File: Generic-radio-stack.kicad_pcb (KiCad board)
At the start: 2 copper layers, 104 parts, among them J1 USB_B_Mini, J2 Conn_01x02, SW1 SW_Push_LED, SW2 SW_Push_LED, SW3 SW_Push_LED, SW4 SW_Push_LED, U1 NCP1117-3.3_SOT223, U10 MAX7219, U11 5_digit_7_segment_display, U12 MAX7219, U13 5_digit_7_segment_display, U14 MAX7219, U15 5_digit_7_segment_display, U16 MAX7219, U17 5_digit_7_segment_display, U18 RP2040, U19 LSF0204PWR, U2 MAX7219, U20 W25Q128JVS, U3 6_digit_7_segment_display_1, U4 MAX7219, U5 6_digit_7_segment_display_1, U6 MAX7219, U7 6_digit_7_segment_display_1, U8 MAX7219, U9 6_digit_7_segment_display_1, Y1 ABLS-12.000MHZ-B4-T

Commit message: Board layout begins. Ugh.
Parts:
- C10, C11, C12, C13, C14, C15, C16, C17, C18, C3, C4, C5, C6, C7, C8, C9, R1, R10, R11, R12, R13, R14, R15, R16, R17, R2, R3, R4, U10, U12, U14, U16, U2, U4, U6, U8: moved to B.Cu
- moved C2 269.2 mm to (462.8, 121.3)
- moved C24 269.2 mm to (477.8, 136.3)
- moved C29 269.2 mm to (471.5, 140.4)
- moved C31 269.2 mm to (471.5, 142.4)
- moved ENC1 269.2 mm to (404.9, 131.2)
- moved R21 269.2 mm to (416.7, 120.4)
- moved R28 269.2 mm to (477.8, 138.3)
- moved R37 269.2 mm to (471.5, 144.5)
- moved U18 269.2 mm to (475.2, 130.6)
- moved U19 269.2 mm to (459.3, 142.3)
- moved C19 269.2 mm to (465.2, 142.5)
- moved C21 269.2 mm to (468.4, 142.5)
- moved C22 269.2 mm to (465.2, 140.4)
- moved C23 269.2 mm to (474.6, 138.3)
- moved C25 269.2 mm to (487.7, 127.0)
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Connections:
- R2 pad 1: COM2_INPUT -> (no net)
- R2 pad 2: Net-(D2-Pad2) -> (no net)
- SW3 pad 1: GND -> (no net)
- SW3 pad 2: COM2_XFR -> (no net)
- SW3 pad 3: Net-(R8-Pad2) -> (no net)
- SW3 pad 4: GND -> (no net)
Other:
- board outline added: 225 x 60 mm

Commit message: Added dual encoder 3d model, fit everything on the board
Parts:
- removed the U8 at (111.9, 96.3)
- added U12: 5_digit_7_segment_display, Generic-radio-stack:5 digit (3+2) 7 segment LED display, F.Cu at (169.0, 65.0)
- C1, C19, C2, C20, C21, C22, C23, C24, C25, C26, C27, C28, C29, C30, C31, C32, D5, J1, J2, R18, R19, R20, R21, R22, R23, R24, R25, R26, R27, R28, R29, R30, R31, R32, R33, R34, R35, R36, R37, R38, R5, R6, R7, R8, R9, Y1: moved to B.Cu
- D1, D2, D3, D4: footprint LED_THT:LED_D5.0mm -> LED_THT:LED_D3.0mm
- U10: value MAX7219 -> 6_digit_7_segment_display_1; footprint Package_SO:SOIC-24W_7.5x15.4mm_P1.27mm -> Generic-radio-stack:6 digit (3+3) 7 segment LED display; moved to F.Cu
- U11: value 5_digit_7_segment_display -> MAX7219; footprint Generic-radio-stack:5 digit (3+2) 7 segment LED display -> Package_SO:SOIC-24W_7.5x15.4mm_P1.27mm; moved to B.Cu
- U19: renamed from U18; moved to B.Cu
- U2: renamed from U1; moved to B.Cu
- U20: renamed from U19; moved to B.Cu
- U21: renamed from U20; moved to B.Cu
- U9: value 6_digit_7_segment_display_1 -> MAX7219; footprint Generic-radio-stack:6 digit (3+3) 7 segment LED display -> Package_SO:SOIC-24W_7.5x15.4mm_P1.27mm; moved to B.Cu
- moved R8 408.8 mm to (89.5, 84.0), turned to 180 degrees
- moved R6 407.1 mm to (89.4, 65.0), turned to 180 degrees
- moved C1 367.0 mm to (123.0, 51.5), turned to -90 degrees
- moved C25 366.6 mm to (122.9, 90.7), turned to 180 degrees
- moved C20 360.3 mm to (126.0, 92.8), turned to 180 degrees
- moved R34 360.3 mm to (126.0, 94.8), turned to 180 degrees
- moved R38 360.3 mm to (126.0, 90.7), turned to 180 degrees
- moved U2 355.5 mm to (129.0, 51.5), turned to 180 degrees
- moved C26 354.1 mm to (129.2, 94.8), turned to 180 degrees
- moved C27 354.1 mm to (129.2, 92.8), turned to 180 degrees
- moved R29 354.1 mm to (129.2, 96.9), turned to 180 degrees
- moved R36 354.1 mm to (129.2, 90.7), turned to 180 degrees
- moved R31 353.2 mm to (129.6, 100.0), turned to 180 degrees
- moved R5 352.6 mm to (149.0, 50.5), turned to 90 degrees
- moved C24 346.9 mm to (132.8, 100.0), turned to 180 degrees
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- renumbered U12 to U13, U13 to U14, U14 to U15, U15 to U16, U16 to U17, U17 to U18, U2 to U3, U3 to U4, U4 to U5, U5 to U6, U6 to U7, U7 to U8
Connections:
- R2 pad 1: (no net) -> COM2_INPUT
- R2 pad 2: (no net) -> Net-(D2-Pad2)
- SW3 pad 1: (no net) -> GND
- SW3 pad 2: (no net) -> COM2_XFR
- SW3 pad 3: (no net) -> Net-(R8-Pad2)
- SW3 pad 4: (no net) -> GND
- U10 pad 1: /5-digit display/DIN -> /6-digit display3/E
- U10 pad 10: unconnected-(U10-Pad10) -> /6-digit display3/F
- U10 pad 11: /5-digit display/DIG_1 -> /6-digit display3/A
- U10 pad 12: LED_LOAD -> /6-digit display3/DIG_5
- U10 pad 13: LED_CLOCK -> /6-digit display3/E
- U10 pad 14: /5-digit display/A -> /6-digit display3/D
- U10 pad 15: /5-digit display/F -> /6-digit display3/DP
- U10 pad 16: /5-digit display/B -> /6-digit display3/C
- U10 pad 17: /5-digit display/G -> /6-digit display3/G
- U10 pad 19: +5V -> /6-digit display3/B
- U10 pad 2: /5-digit display/DIG_0 -> /6-digit display3/D
- U10 pad 20: /5-digit display/C -> /6-digit display3/DIG_0
- U10 pad 21: /5-digit display/E -> /6-digit display3/DIG_1
- U10 pad 22: /5-digit display/DP -> /6-digit display3/F
- U10 pad 23: /5-digit display/D -> /6-digit display3/A
- U10 pad 24: /5-digit display/DOUT -> /6-digit display3/DIG_2
- U10 pad 3: /5-digit display/DIG_4 -> /6-digit display3/DP
- U10 pad 4: GND -> /6-digit display3/C
- U10 pad 5: unconnected-(U10-Pad5) -> /6-digit display3/G
- U10 pad 7: /5-digit display/DIG_3 -> /6-digit display3/B
- U10 pad 8: unconnected-(U10-Pad8) -> /6-digit display3/DIG_3
- U10 pad 9: GND -> /6-digit display3/DIG_4
- U11 pad 1: /5-digit display/E -> /5-digit display/DIN
- U11 pad 10: /5-digit display/F -> unconnected-(U11-Pad10)
- U11 pad 11: /5-digit display/A -> /5-digit display/DIG_1
- U11 pad 12: /5-digit display/DIG_4 -> LED_LOAD
- U11 pad 13: /5-digit display/E -> LED_CLOCK
- U11 pad 14: /5-digit display/D -> /5-digit display/A
- U11 pad 15: /5-digit display/C -> /5-digit display/F
- U11 pad 16: /5-digit display/G -> /5-digit display/B
- U11 pad 17: /5-digit display/DP -> /5-digit display/G
- U11 pad 18: /5-digit display/DIG_0 -> Net-(R14-Pad1)
- U11 pad 19: /5-digit display/A -> +5V
- U11 pad 2: /5-digit display/D -> /5-digit display/DIG_0
- U11 pad 20: /5-digit display/B -> /5-digit display/C
- U11 pad 21: /5-digit display/DIG_1 -> /5-digit display/E
- U11 pad 22: /5-digit display/F -> /5-digit display/DP
- U11 pad 3: /5-digit display/DP -> /5-digit display/DIG_4
- U11 pad 4: /5-digit display/C -> GND
- U11 pad 5: /5-digit display/G -> unconnected-(U11-Pad5)
- U11 pad 7: /5-digit display/B -> /5-digit display/DIG_3
- U11 pad 8: /5-digit display/DIG_2 -> unconnected-(U11-Pad8)
- U11 pad 9: /5-digit display/DIG_3 -> GND
- U9 pad 1: /6-digit display3/E -> /6-digit display2/DOUT
- U9 pad 10: /6-digit display3/F -> /6-digit display3/DIG_5
- U9 pad 11: /6-digit display3/A -> /6-digit display3/DIG_1
- U9 pad 12: /6-digit display3/DIG_5 -> LED_LOAD
- U9 pad 13: /6-digit display3/E -> LED_CLOCK
- U9 pad 14: /6-digit display3/D -> /6-digit display3/A
- U9 pad 15: /6-digit display3/DP -> /6-digit display3/F
- U9 pad 16: /6-digit display3/C -> /6-digit display3/B
- U9 pad 19: /6-digit display3/B -> +5V
- U9 pad 2: /6-digit display3/D -> /6-digit display3/DIG_0
- U9 pad 20: /6-digit display3/DIG_0 -> /6-digit display3/C
- U9 pad 21: /6-digit display3/DIG_1 -> /6-digit display3/E
- U9 pad 22: /6-digit display3/F -> /6-digit display3/DP
- U9 pad 23: /6-digit display3/A -> /6-digit display3/D
- U9 pad 24: /6-digit display3/DIG_2 -> /5-digit display3/DIN
- U9 pad 3: /6-digit display3/DP -> /6-digit display3/DIG_4
- U9 pad 4: /6-digit display3/C -> GND
- U9 pad 5: /6-digit display3/G -> unconnected-(U9-Pad5)
- U9 pad 7: /6-digit display3/B -> /6-digit display3/DIG_3
- U9 pad 8: /6-digit display3/DIG_3 -> unconnected-(U9-Pad8)
- U9 pad 9: /6-digit display3/DIG_4 -> GND
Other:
- board size 225 x 60 mm -> 225 x 66.5 mm

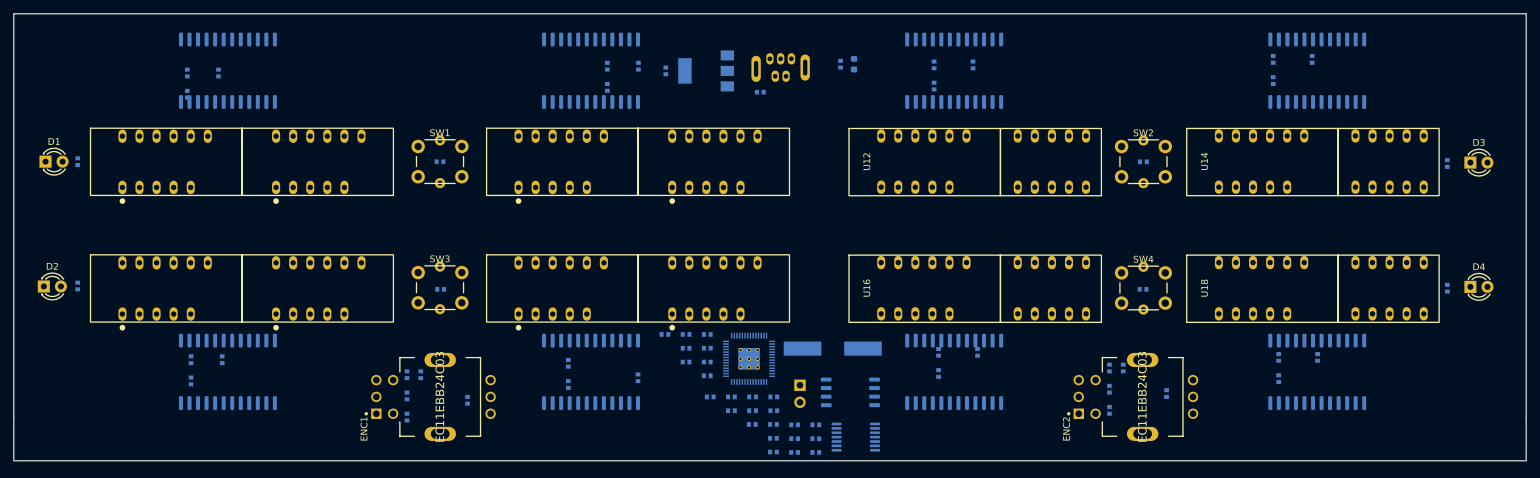
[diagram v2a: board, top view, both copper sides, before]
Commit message: Add mounting holes
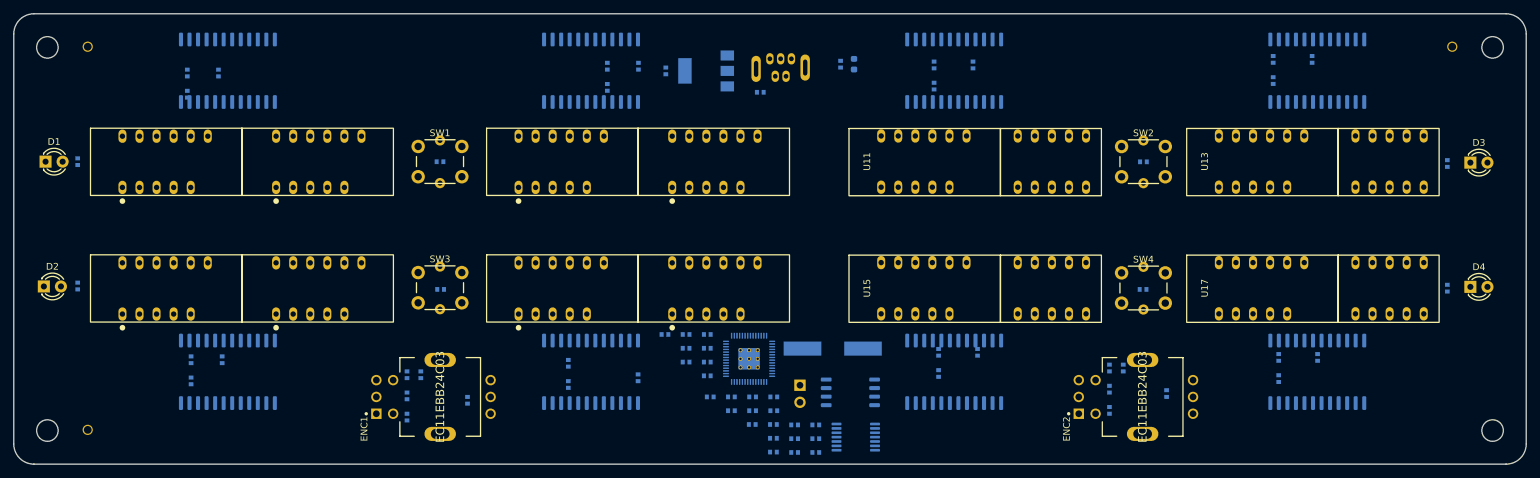
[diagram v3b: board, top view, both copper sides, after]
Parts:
- added H1: MountingHole, MountingHole:MountingHole_3.2mm_M3, F.Cu at (31.0, 48.0)
- added H2: MountingHole, MountingHole:MountingHole_3.2mm_M3, F.Cu at (246.0, 48.0)
- added H3: MountingHole, MountingHole:MountingHole_3.2mm_M3, F.Cu at (31.0, 105.0)
- added H4: MountingHole, MountingHole:MountingHole_3.2mm_M3, F.Cu at (246.0, 105.0)
- added H5: MountingHole, Generic-radio-stack:JLCPCB_Tooling_Hole, F.Cu at (37.0, 48.0)
- added H6: MountingHole, Generic-radio-stack:JLCPCB_Tooling_Hole, F.Cu at (240.0, 48.0)
- added H7: MountingHole, Generic-radio-stack:JLCPCB_Tooling_Hole, F.Cu at (37.0, 105.0)
- renumbered U2 to U1, U11 to U10, U12 to U11, U13 to U12, U14 to U13, U15 to U14, U16 to U15, U17 to U16, U18 to U17, U19 to U18, U20 to U19, U3 to U2, U21 to U20, U4 to U3, U5 to U4, U6 to U5, U7 to U6, U8 to U7, U9 to U8, U10 to U9
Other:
- board size 225 x 66.5 mm -> 225 x 67 mm

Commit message: initial routing of RP2040
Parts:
- moved J2 246.8 mm to (388.7, 121.3)
- moved R31 225.7 mm to (355.1, 110.5)
- moved R34 217.4 mm to (342.4, 115.6)
- moved R38 213.4 mm to (338.1, 114.6)
- moved R36 210.4 mm to (338.6, 111.3)
- moved R37 203.4 mm to (342.4, 112.3)
- moved U19 197.9 mm to (349.0, 112.8)
- moved R32 197.4 mm to (342.7, 110.2)
- moved R33 182.0 mm to (323.3, 121.4)
- moved R35 180.5 mm to (315.5, 122.2)
- moved C32 177.1 mm to (318.8, 121.2)
- moved U20 171.9 mm to (320.0, 127.3)
- moved C20 61.3 mm to (158.6, 144.7), turned to 0 degrees
- moved Y1 58.2 mm to (159.8, 149.8)
- moved C27 56.2 mm to (164.7, 136.3), turned to 0 degrees
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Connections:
- net Net-(R28-Pad2) renamed /RP2040/XOUT
- net Net-(R29-Pad1) renamed /RP2040/D+
- net Net-(R30-Pad1) renamed /RP2040/D-
- C19 pad 2: Net-(C19-Pad2) -> /RP2040/XIN
- U18 pad 20: Net-(C19-Pad2) -> /RP2040/XIN
- U18 pad 44: GND -> +3V3
- Y1 pad 1: Net-(C20-Pad2) -> /RP2040/XIN
- Y1 pad 2: Net-(C19-Pad2) -> Net-(C20-Pad2)
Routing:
- net +3V3: track 0.00 -> 28.5 mm
- net +1V1: track 0.00 -> 18.7 mm, vias 0 -> 4
- net /RP2040/XIN: track 0.00 -> 13.3 mm
- net Net-(C20-Pad2): track 0.00 -> 8.12 mm
- net /RP2040/XOUT: track 0.00 -> 4.23 mm
- net /RP2040/D-: track 0.00 -> 3.44 mm
- net /RP2040/D+: track 0.00 -> 3.19 mm
- added copper zone on B.Cu, net +1V1
- added copper zone on B.Cu, net +3V3

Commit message: More RP2040 routing
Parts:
- moved C32 156.0 mm to (162.8, 118.1), turned to 0 degrees
- moved R33 155.0 mm to (168.4, 117.6), turned to -90 degrees
- moved U20 154.3 mm to (165.9, 122.4)
- moved R35 145.9 mm to (169.7, 117.6), turned to -90 degrees
- moved C2 76.7 mm to (143.8, 131.1)
- moved U1 75.8 mm to (144.3, 125.7), turned to -90 degrees
- moved C1 72.6 mm to (146.1, 120.4), turned to 180 degrees
- moved J1 67.8 mm to (156.2, 116.8), turned to 0 degrees
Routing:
- net GND: track 0.00 -> 24.0 mm, vias 0 -> 18
- net /RP2040/QSPI_SS: track 0.00 -> 24.0 mm
- net /RP2040/QSPI_SD1: track 0.00 -> 18.2 mm
- net /RP2040/QSPI_SD2: track 0.00 -> 13.8 mm
- net /RP2040/QSPI_SD3: track 0.00 -> 11.7 mm
- net /RP2040/QSPI_SCLK: track 0.00 -> 10.6 mm
- net /RP2040/QSPI_SD0: track 0.00 -> 8.72 mm
- net +3V3: track 28.5 -> 33.1 mm
- net +5V: track 0.00 -> 2.19 mm
- added copper zone on B.Cu, net GND

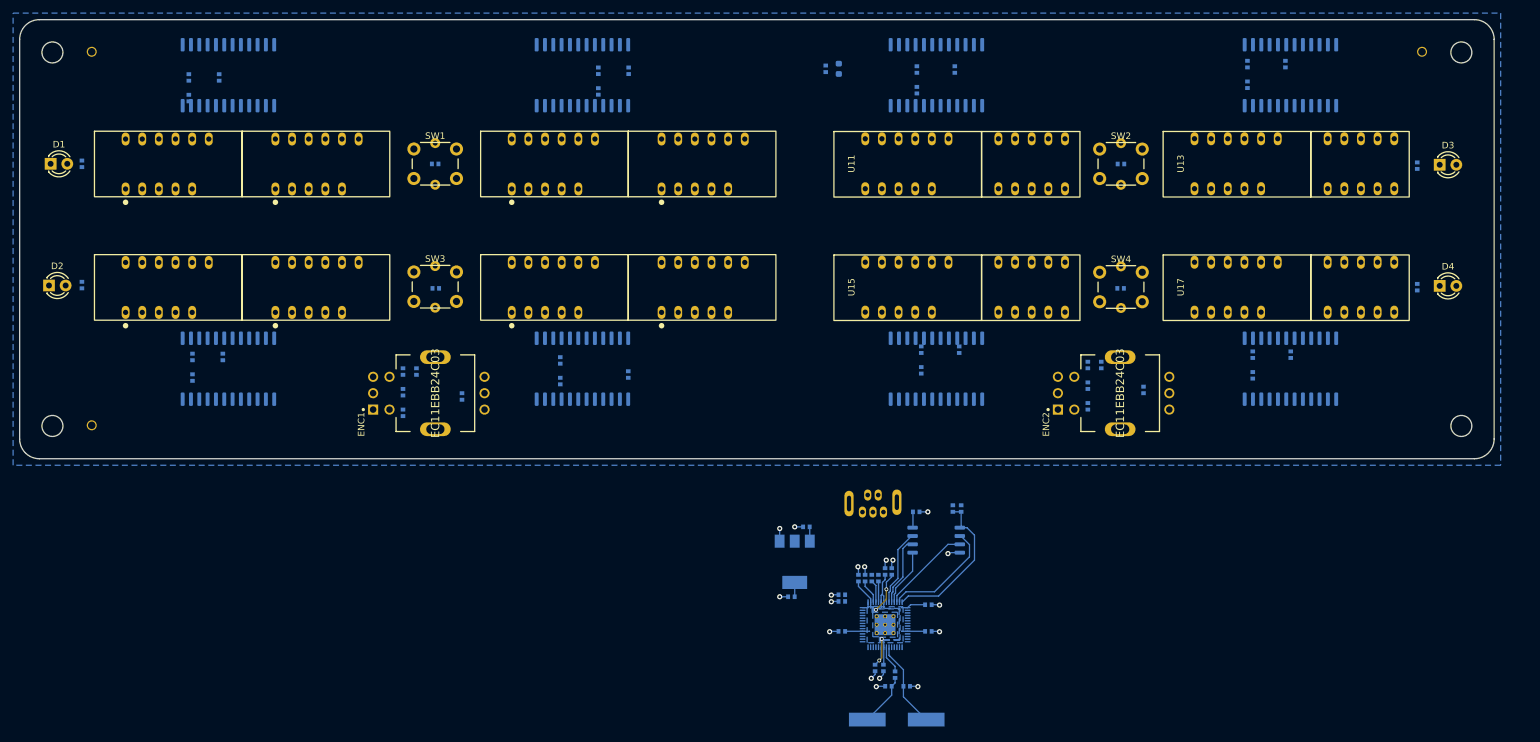
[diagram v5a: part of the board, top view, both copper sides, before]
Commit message: New USB footprint
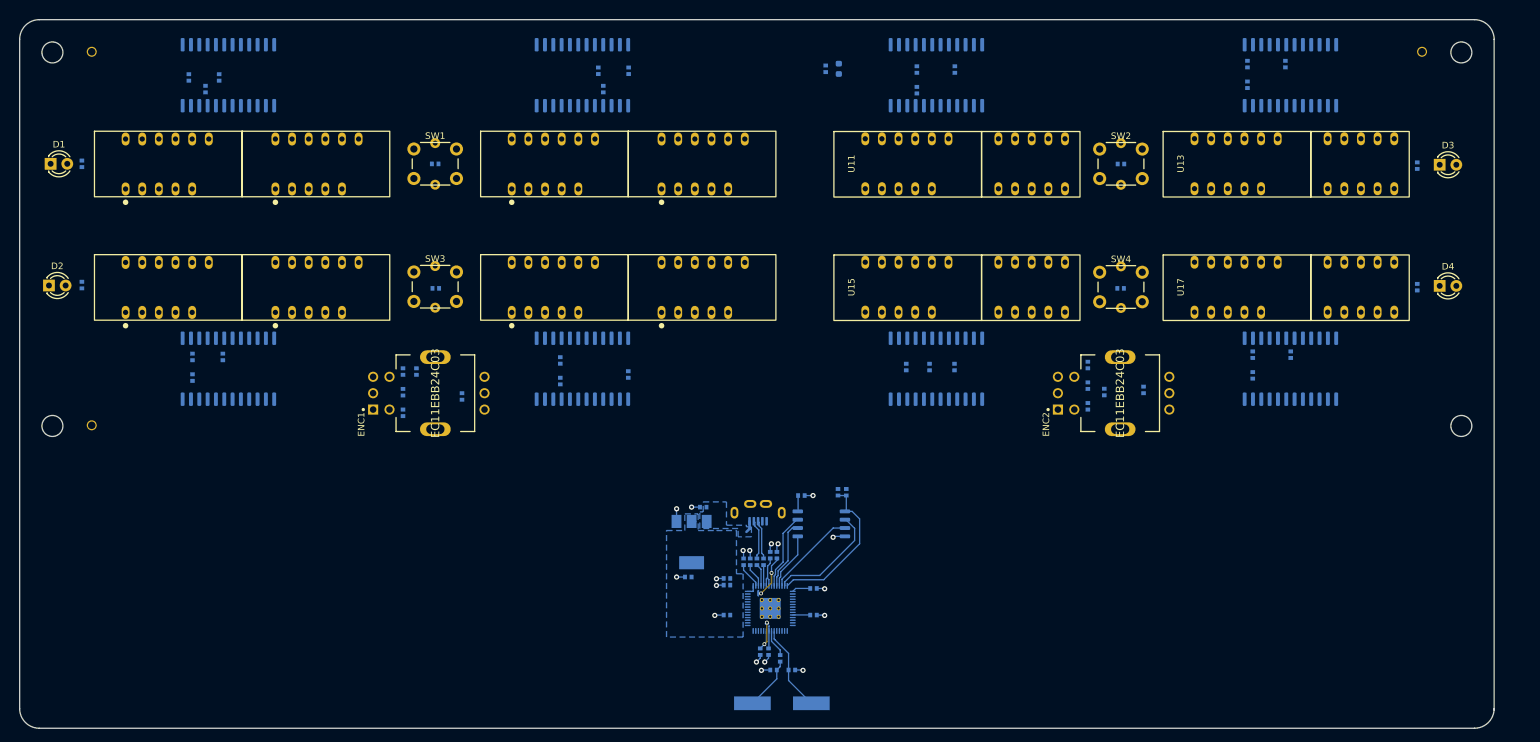
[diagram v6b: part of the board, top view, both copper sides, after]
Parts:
- J1: value USB_B_Mini -> USB_B_Micro; footprint Generic-radio-stack:USB_B_Mini_Amphenol_UE25BE5510H -> Generic-radio-stack:ZX80-B-5P
- moved C22 17.7 mm to (139.0, 139.4)
- moved C28 17.7 mm to (140.3, 139.4)
- moved R28 17.7 mm to (142.1, 140.5)
- moved C20 17.7 mm to (141.0, 142.2)
- moved C23 17.7 mm to (137.5, 125.7)
- moved C24 17.7 mm to (136.5, 125.7)
- moved C25 17.7 mm to (140.5, 124.7)
- moved R29 17.7 mm to (139.5, 125.7)
- moved R35 17.7 mm to (152.1, 115.1)
- moved U18 17.7 mm to (140.5, 132.8)
- moved Y1 17.7 mm to (142.3, 147.3)
- moved C19 17.7 mm to (143.8, 142.2)
- moved C21 17.7 mm to (141.6, 124.7)
- moved C26 17.7 mm to (147.1, 129.8)
- moved C27 17.7 mm to (147.1, 133.9)
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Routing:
- net +3V3: track 33.1 -> 23.5 mm
- net D-: track 0.00 -> 6.11 mm
- net D+: track 0.00 -> 6.03 mm
- added copper zone on B.Cu, net +5V
- removed copper zone on B.Cu, net GND
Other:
- board size 225 x 67 mm -> 225 x 108.1 mm
